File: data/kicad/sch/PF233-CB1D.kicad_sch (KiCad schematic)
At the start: 64 parts, among them M5 5 V 1.5 A switching module, U1 Pico 2 W

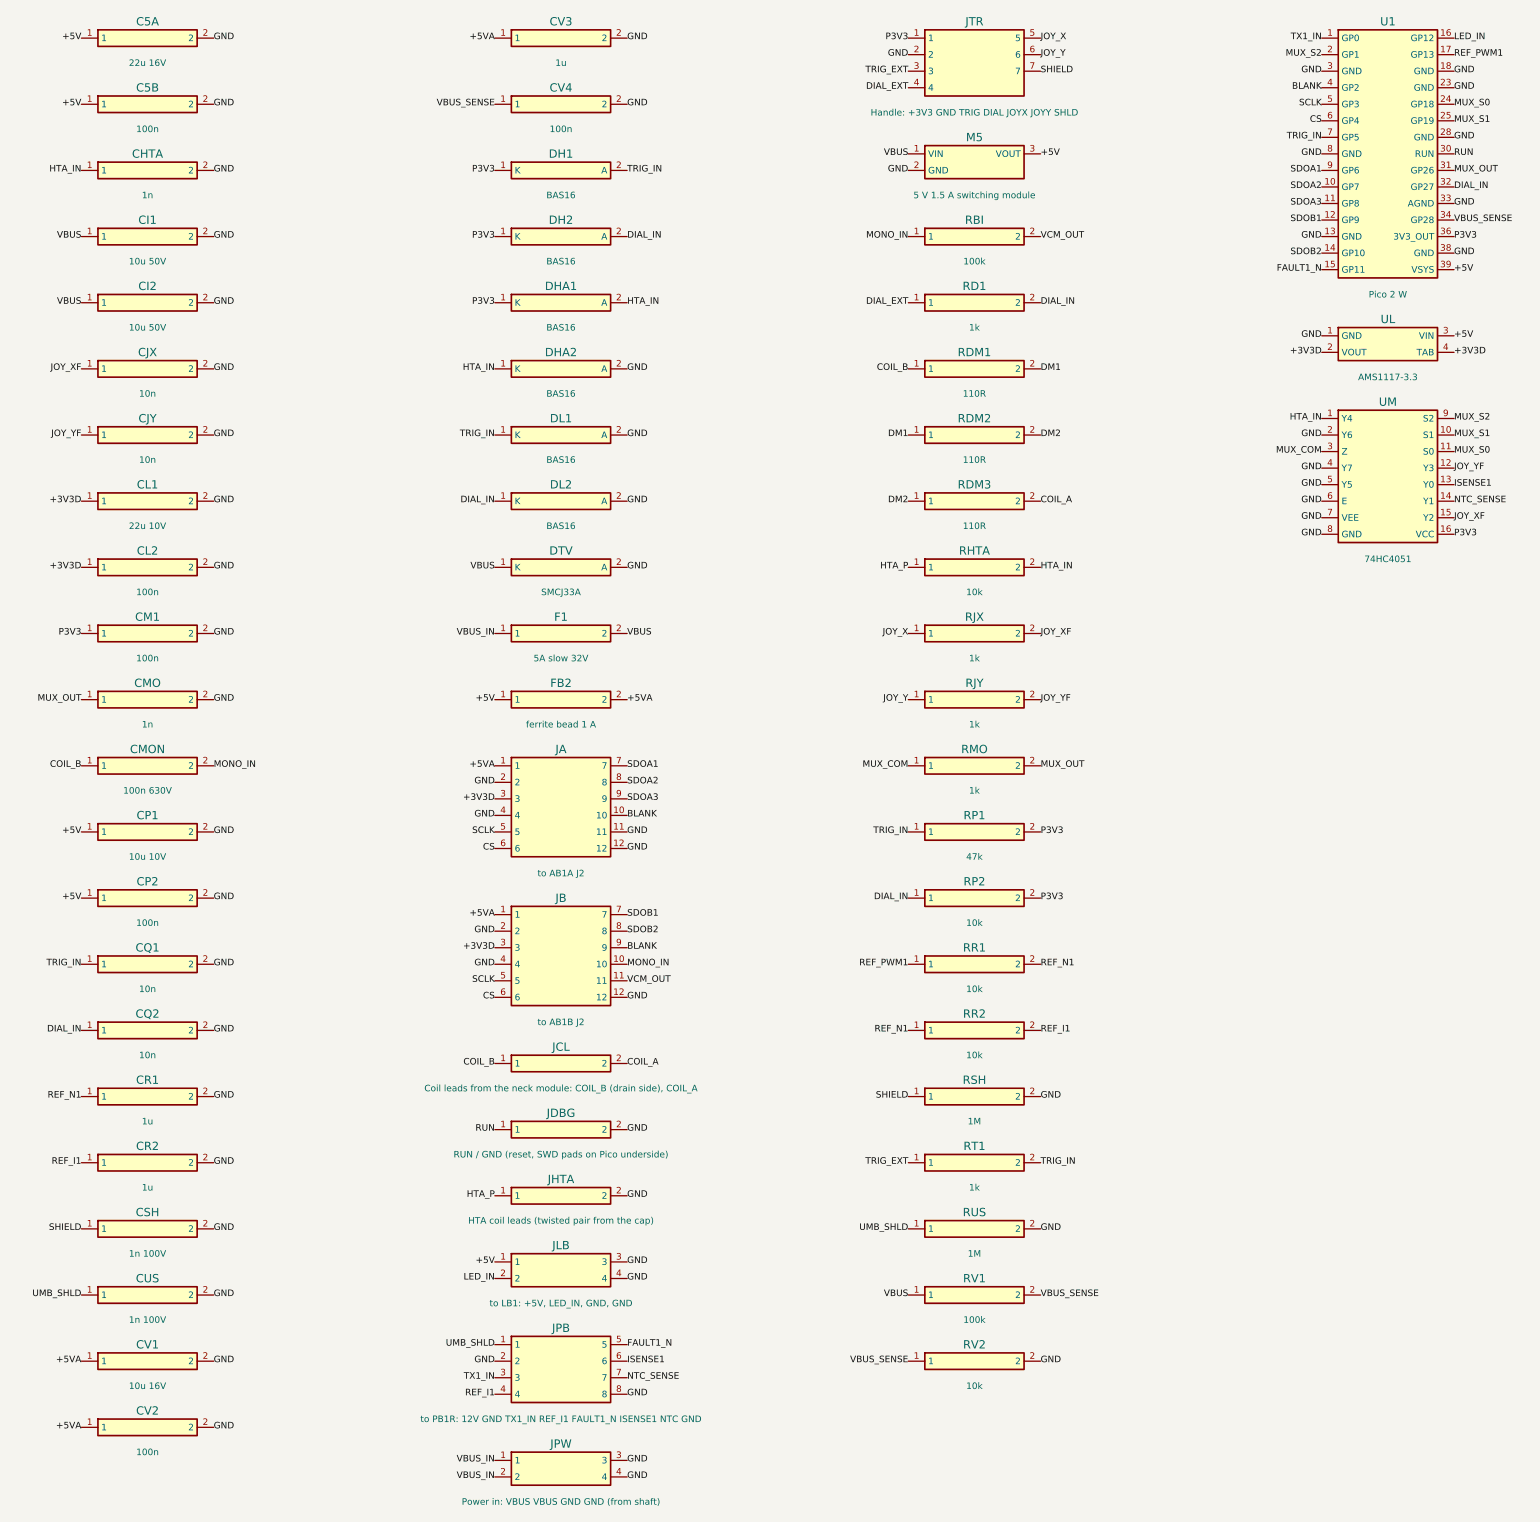
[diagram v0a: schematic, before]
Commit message: External KiCad 9 DRC, CB1D-B revision, HV plane keep-out, router/export fixes (step 1 of the transmit-region sign-off)
- KiCad 9.0.9 installed; kicad_drc.py (zone fill, design rules, automatic negative control), dru_gen.py (last rule wins), make kicad-drc
- CB1D-B: MONO 460 V tap and joystick inputs removed, parts kept inside the rib annulus; 58 parts, 41/41 nets, 1669 mm, 101 vias
- CB1D and LB1: KiCad 0 errors / 0 unconnected; independent DRC 0/0; head cross-check 0 fail; wiring audit clean
- gerber_out: 1.0 mm plane keep-out for HV pads and vias (gerber_hv_check.py, control proves the old writer failed 8/8)
- route_fix: nearest-pad stubs, circle test for round pads, duplicate vias; kicad_inject: template zones no longer kept
- new Gerbers CB1D_B and LB1_v4; CB1D_v2 and LB1_v3_stubbed marked superseded
- regress 39 pass; CORRECTIONS, DESIGN_STATE, OPEN_ITEMS 20/23/24, ASSUMPTIONS 30

Not done: PB1R routing, TXJ1 edge clearance, SB1R annular rings, CAM viewer, datasheets, bench test.

Co-Authored-By: Claude Sonnet 5.5 <noreply@anthropic.com>
Claude-Session: https://claude.ai/code/session_01T7iU5pGiBfkKRBbe2JcTJx
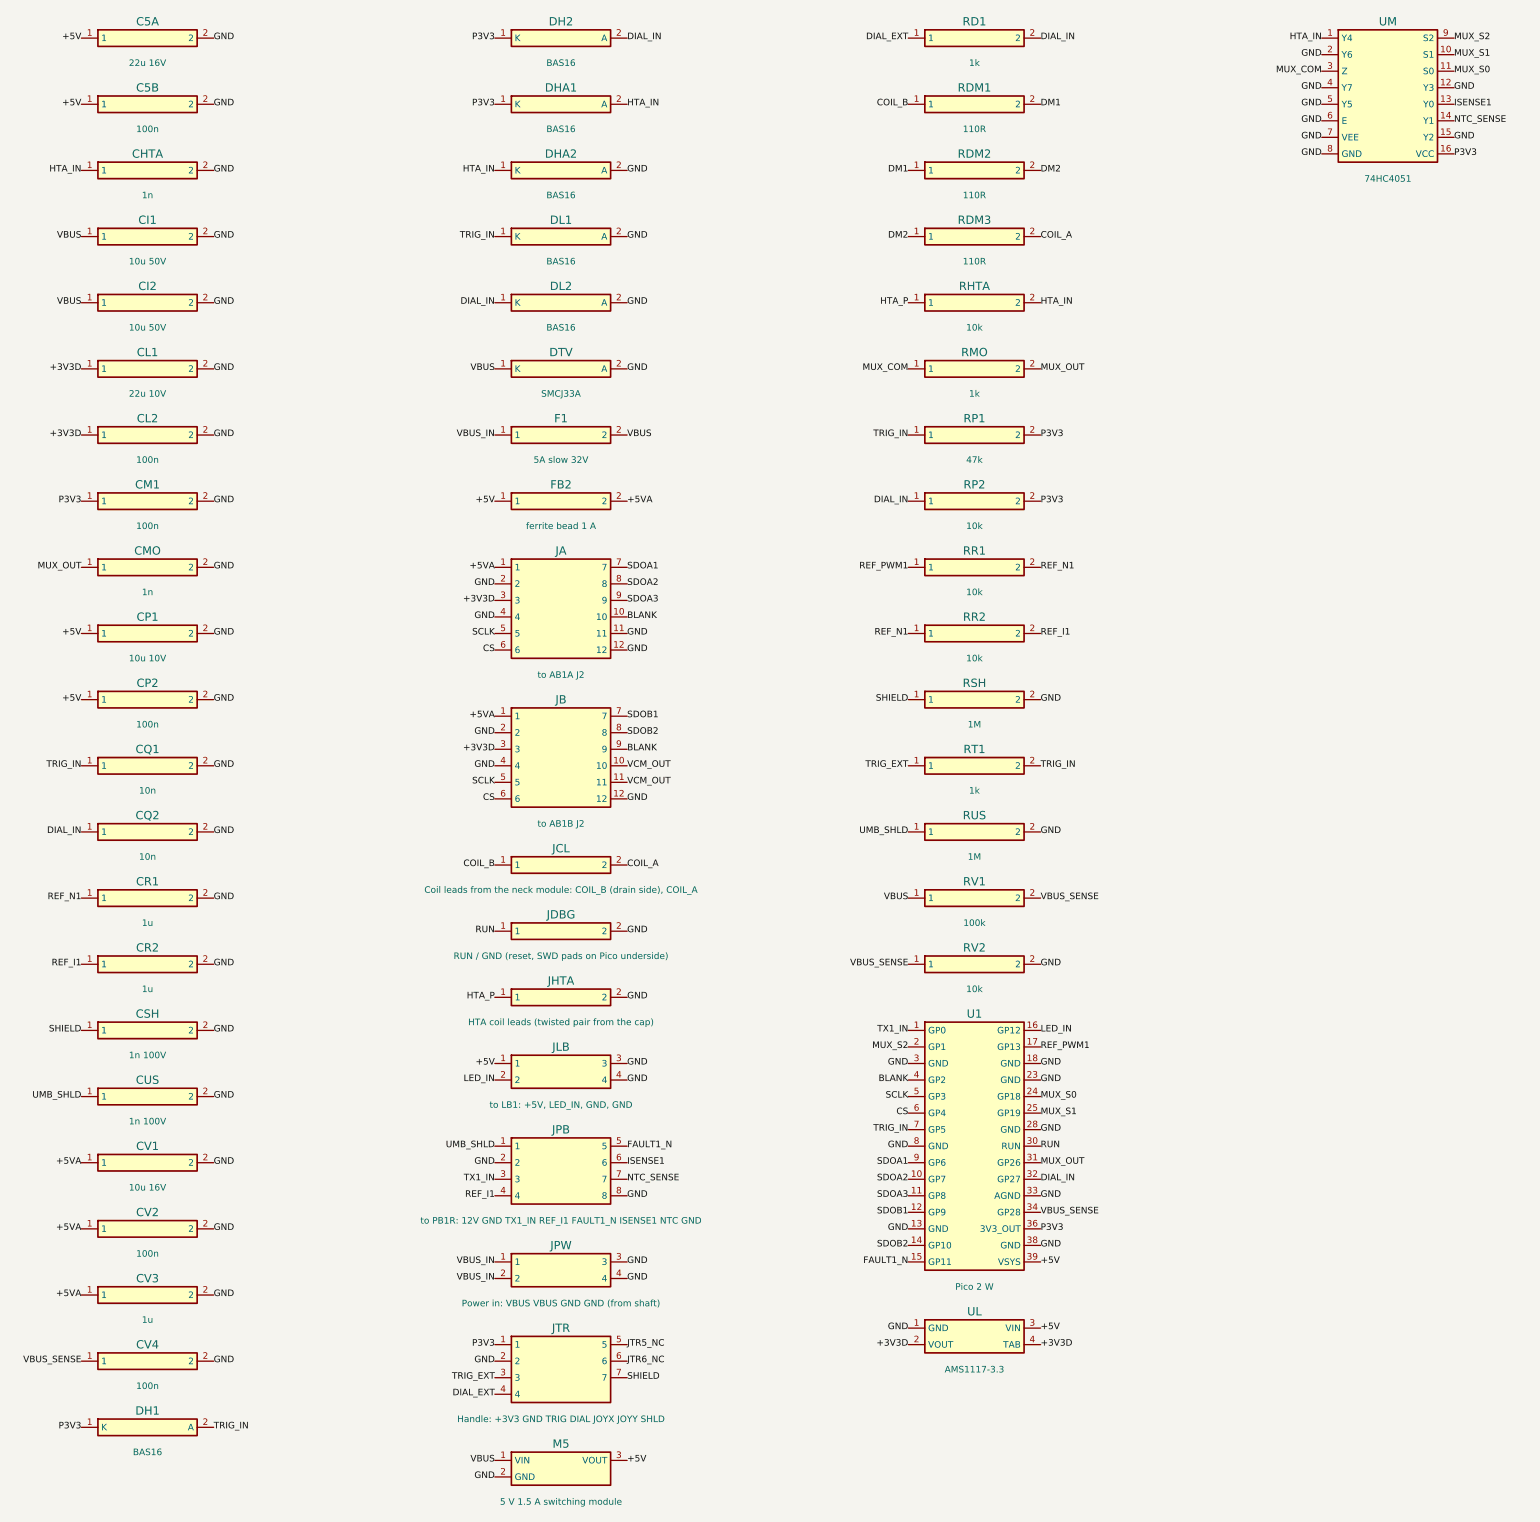
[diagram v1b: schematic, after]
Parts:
- removed CJX: 10n, Capacitor_SMD:C_0603_1608Metric, symbol PF233_auto:CJX
- removed CJY: 10n, Capacitor_SMD:C_0603_1608Metric, symbol PF233_auto:CJY
- removed CMON: 100n 630V, Capacitor_SMD:C_1210_3225Metric, symbol PF233_auto:CMON
- removed RBI: 100k, Resistor_SMD:R_0603_1608Metric, symbol PF233_auto:RBI
- removed RJX: 1k, Resistor_SMD:R_0603_1608Metric, symbol PF233_auto:RJX
- removed RJY: 1k, Resistor_SMD:R_0603_1608Metric, symbol PF233_auto:RJY
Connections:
- net JOY_XF is gone; now on net GND: UM.15 (Y2)
- net JOY_YF is gone; now on net GND: UM.12 (Y3)
- net MONO_IN is gone; now on net VCM_OUT: JB.10
- net JOY_X renamed JTR5_NC
- net JOY_Y renamed JTR6_NC
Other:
- moved on the sheet: CL1, CL2, CM1, CMO, CP1, CP2, CQ1, CQ2, CR1, CR2, CSH, CUS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

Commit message: Step 2: CB1D options, SB1R via drill, TXJ1 pads, fab-floor rules, finishes (KiCad 9: 5 boards, 0 errors / 0 unconnected)
- SB1R: via drill 0.4 mm (was 0.8 = no annular ring in the KiCad files and the PTH drill files); QB transfer nets QB_T1/QB_T2; Gerbers SB1R_QA_v2 / SB1R_QB_v2, old marked superseded; sbq sims unchanged (0 numbers moved)
- TXJ1: AWG12 pads 3.8 mm (edge distance 0.6 mm); Gerbers TXJ1_v2
- CB1D: RJB10 0R fitted on JB.10, RJ5/RJ6 DNP grounds for JTR.5/.6 (61 parts, 44/44 nets); Gerbers CB1D_B2; wiring alias JB10_VCM
- dru_gen: conservative Advanced Circuits / TTM floor (UNVERIFIED), SB1R keys; no ENIG near the coil/receivers (immersion silver / HASL); docs/design/FAB_RULES.md
- make kicad-drc covers CB1D, LB1, TXJ1, SB1R-QA/QB; regress 42 pass; CORRECTIONS, DESIGN_STATE, OPEN_ITEMS 23/25-27, ASSUMPTIONS 31

Co-Authored-By: Claude Sonnet 5.5 <noreply@anthropic.com>
Claude-Session: https://claude.ai/code/session_01T7iU5pGiBfkKRBbe2JcTJx
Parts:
- added RJ5: 0R DNP, Resistor_SMD:R_0603_1608Metric, symbol PF233_auto:RJ5
- added RJ6: 0R DNP, Resistor_SMD:R_0603_1608Metric, symbol PF233_auto:RJ6
- added RJB10: 0R, Resistor_SMD:R_0603_1608Metric, symbol PF233_auto:RJB10
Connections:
- net GND: now also RJ5.2, RJ6.2
- net VCM_OUT: now also RJB10.2; no longer JB.10
- net JTR5_NC renamed JTR5_OPT
- net JTR5_OPT: now also RJ5.1
- net JTR6_NC renamed JTR6_OPT
- net JTR6_OPT: now also RJ6.1
- new net JB10_VCM: JB.10, RJB10.1
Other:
- moved on the sheet: RMO, RP1, RP2, RR1, RR2, RSH, RT1, RUS, RV1, RV2, U1, UL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

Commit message: Step 5: datasheets and fabricator sheets (vendor-derived floor, verified parts, PB1R 9-can bank, Gerber edge read-back)
- Fab floor from AdvancedPCB / TTM pages (docs/design/FAB_RULES_VERIFIED.md, U-FAB-RULES closed): clearance 0.16,
  component-PTH ring 0.18 / hole 0.46, drill-copper 0.26, drill-drill 0.41, every rule (severity error).
  CB1D JA/JB and HB2 TO-92 pads 1.02 mm; route_fix merges close same-net vias (CB1D, LB1).
- Parts from manufacturer PDFs (docs/design/DATASHEET_LOG.md): PB1R bulk 9 x Panasonic EEHZC1H101P
  (the 150 uF / 50 V polymer-Ta was not found; bank stays 900 uF, on-time table unchanged), PB1R re-placed
  with the Kelvin/comparator cluster pinned (pulse path 4.9 mohm, spike 7.5 V, ground ref 15.5 mV unchanged);
  SMCJ30A (SMCJ33A clamps 53.3 V > 50 V parts), Si4401FDY, BZT52C15, Bourns SF-1206S500-2 (new 1206 land),
  DRV5023BIQLPG, CRCW2512 500 V, OPA2365/OPA2211/LM393/CD74HC4051 checked. ES3J 600 V kept as a WATCH.
- U-DS-PARTS split into groups; open: TXDRIVE, OKI, PACK, BAV199, HVTERM. U-COLD-BOOTSTRAP closed.
- Controls retargeted to fixture folders (12/12). Netlist date fixed (data changed daily).
- Gerber planes from gerber_out.py ran into the notch and to 0.1 mm of the edge since r1 (found by the
  independent review): fixed, and gerber_edge_check.py reads every copper layer back.
- New Gerber sets CB1D_B3, LB1_v5, PB1R_v2; old sets marked SUPERSEDED.
- Findings for the owner: aluminium cans ~0.5 x a 1 g nugget (OPEN_ITEMS 34), OPA2365 capacitive load (30),
  OPA2211 input range on 5 V (31), Hall magnet spread (32).
- Strict regress 55 PASS / 0 FAIL / 0 SKIP; sign-off 44 PASS / 0 FAIL / 0 SKIP / 19 UNVERIFIED.

Co-Authored-By: Claude Opus 5.5 <noreply@anthropic.com>
Claude-Session: https://claude.ai/code/session_015VKhZtgEAWnezB2NDY75VV
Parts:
- DTV: value SMCJ33A -> SMCJ30A
- F1: footprint Fuse:Fuse_1812_4532Metric -> Fuse:Fuse_1206_3216Metric
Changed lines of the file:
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@@
   (symbol (lib_id "PF233_auto:DTV") (at 93.98 81.28 0) (unit 1) (exclude_from_sim no) (in_bom yes) (on_board yes) (dnp no)
     (property "Reference" "DTV" (at 93.98 78.74 0) (effects (font (size 1.27 1.27))))
-    (property "Value" "SMCJ33A" (at 93.98 85.09 0) (effects (font (size 1.0 1.0))))
+    (property "Value" "SMCJ30A" (at 93.98 85.09 0) (effects (font (size 1.0 1.0))))
     (property "Footprint" "Diode_SMD:D_SMC" (at 93.98 81.28 0) (effects (font (size 1.27 1.27)) hide))
     (pin "1")
@@
     (property "Reference" "F1" (at 93.98 88.90 0) (effects (font (size 1.27 1.27))))
     (property "Value" "5A slow 32V" (at 93.98 95.25 0) (effects (font (size 1.0 1.0))))
-    (property "Footprint" "Fuse:Fuse_1812_4532Metric" (at 93.98 91.44 0) (effects (font (size 1.27 1.27)) hide))
+    (property "Footprint" "Fuse:Fuse_1206_3216Metric" (at 93.98 91.44 0) (effects (font (size 1.27 1.27)) hide))
     (pin "1")
     (pin "2")

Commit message: WIP stage 5: B3/B5/B6/B8 closed in blockers.json, B7 narrowed to HVTERM, B12 opened; cap-v18 pipeline step (cap was not regenerated on a fresh work/); upper_check septum joint by voxels; curated STLs refreshed (U6 dock for the real MT60, septum lap segments, canonical face order); DESIGN_STATE stress counts
Co-Authored-By: Claude Opus 5.5 <noreply@anthropic.com>
Claude-Session: https://claude.ai/code/session_01FX4DWSYYjMCFGGA6gmha65
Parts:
- added RML: 270, Resistor_SMD:R_0603_1608Metric, symbol PF233_auto:RML
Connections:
- net +3V3D: now also RML.1
- net GND: now also RML.2
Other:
- moved on the sheet: RMO, RP1, RP2, RR1, RR2, RSH, RT1, RUS, RV1, RV2, U1, UL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

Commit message: WIP: sign-off re-run outputs (publish in progress)
Co-Authored-By: Claude Opus 5.5 <noreply@anthropic.com>
Claude-Session: https://claude.ai/code/session_01FX4DWSYYjMCFGGA6gmha65
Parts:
- JLB: value to LB1: +5V, LED_IN, GND, GND -> to LB1: +5V, LED_IN, LED_CLK, GND
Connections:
- net GND: no longer JLB.3
- new net LED_CLK: JLB.3, U1.19 (GP14)
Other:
- moved on the sheet: UL, UM
